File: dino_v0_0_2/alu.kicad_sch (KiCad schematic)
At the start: 22 parts, among them U38 74F382N, U40 74F382N, U45 74LS373, U46 74LS373, U47 74LS373, U48 74LS157, U49 74LS273, U50 74LS02, U52 74LS02, U53 74LS08, U77 74LS157

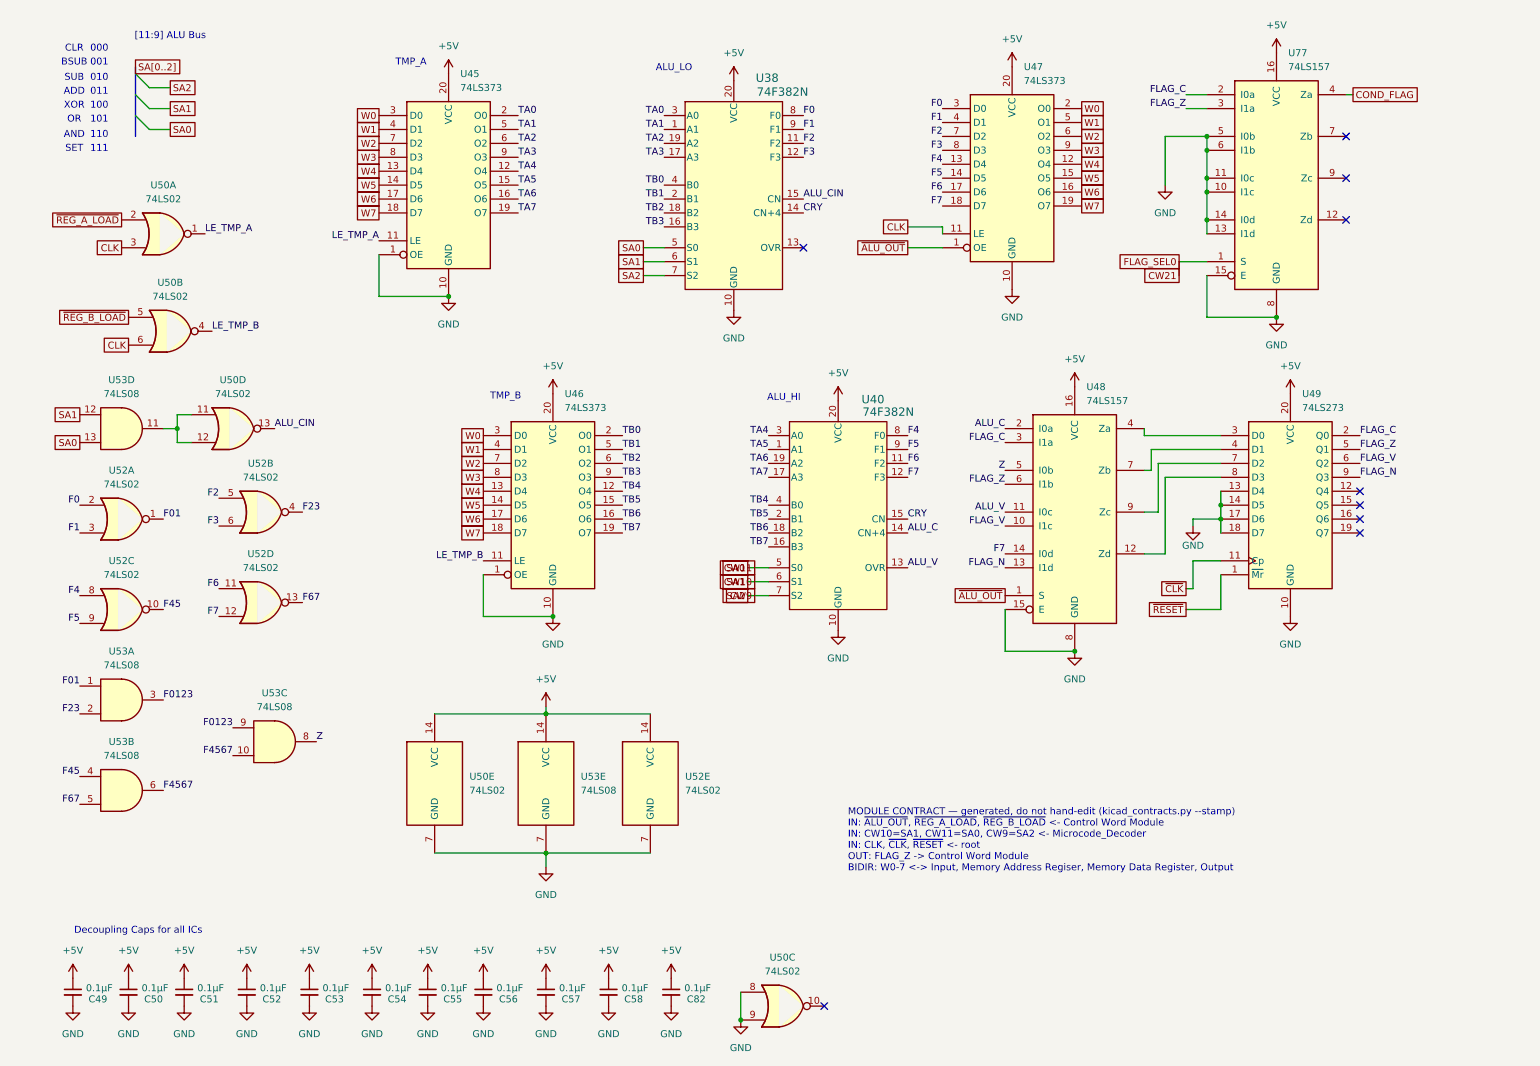
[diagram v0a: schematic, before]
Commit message: feat(int): draw the interrupt block; sheet cleanup pass
New sheet dino_v0_0_2/interrupt.kicad_sch (page 15): U80-U87, R28 4.7k
pull-up on ~{IRQ}, R29 100R on the block's CLK branch, C83-C90. Every
pin per PHASE_INT SECTION 3, checked against the plan with kicad_netlist
and kicad-cli (146 pins, 0 mismatches).

Old sheets (SECTION 3.2): U28.4 lifted off GND to INJECT; U61.3 to
END_OR_ACCEPT; U36.1 to PC_UP_GATED; U49 D0-3 cut from U48 Za-Zd and
routed through U87 as FLAG_NEXT0-3 / FLAG_D0-3; FLAG_C/Z/V/N and the
five decoder outputs made global. dino_serial: U104 74LS05, INTR ->
~{IRQ}, C4.

Placement pass on every sheet: bus entries and global labels no longer
share wires; M, CW, T, IRB and SA buses kept as labelled keys. Nets
diffed against HEAD per sheet: only the intended changes and a rotated
C29. Project ERC: 0 errors. MODULE CONTRACT stamps regenerated.

Co-Authored-By: Claude Fable 5.1 <noreply@anthropic.com>
Claude-Session: https://claude.ai/code/session_01JGxSS4MVUcaZdKZGtKroSg
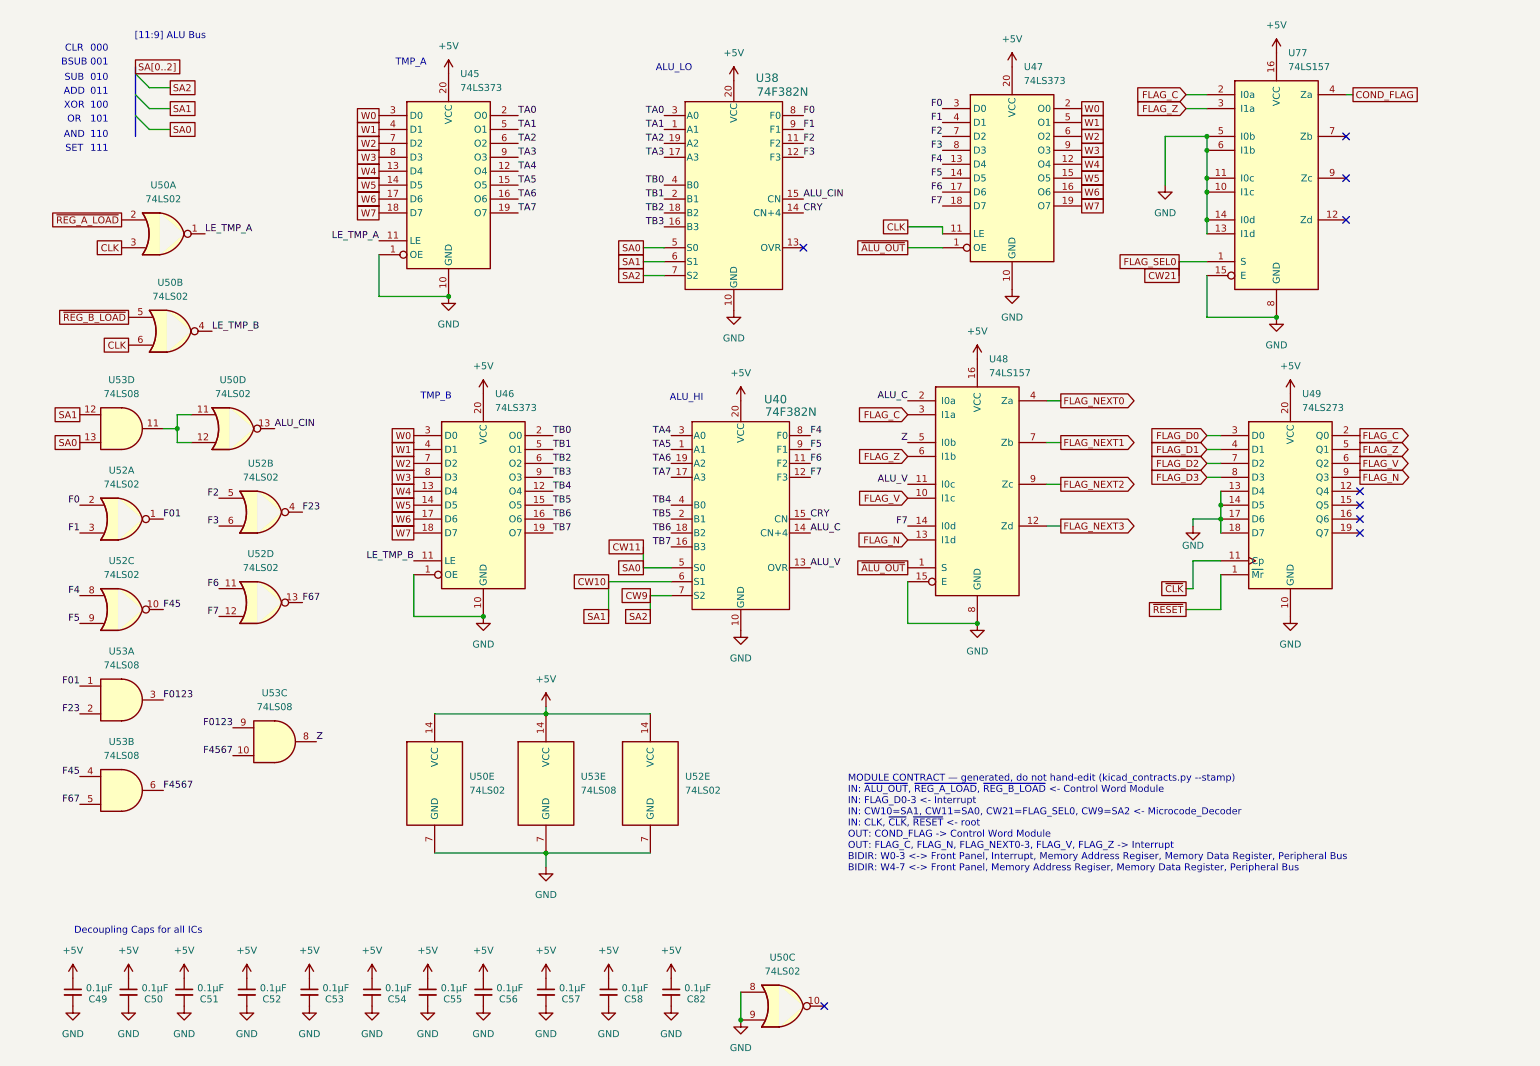
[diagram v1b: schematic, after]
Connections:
- net FLAG_D0: now reaches U49.3 (D0)
- net FLAG_D0: no longer U48.4 (Za)
- net FLAG_D1: now reaches U49.4 (D1)
- net FLAG_D1: no longer U48.7 (Zb)
- net FLAG_D2: now reaches U49.7 (D2)
- net FLAG_D2: no longer U48.9 (Zc)
- net FLAG_D3: now reaches U49.8 (D3)
- net FLAG_D3: no longer U48.12 (Zd)
- new net FLAG_NEXT0: U48.4 (Za)
- new net FLAG_NEXT1: U48.7 (Zb)
- new net FLAG_NEXT2: U48.9 (Zc)
- new net FLAG_NEXT3: U48.12 (Zd)
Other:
- note added: "MODULE CONTRACT — generated, do not hand-edit (kicad_contracts.py --stamp) IN: ~{ALU_OUT}, ~{REG_A_LOAD}, ~{REG_B_LOAD} <- Control Word Module IN: FLAG_D0-3 <- Interrupt IN: CW10=SA1, CW11=SA0, CW21=FLAG_SEL0, CW9=SA2 <- Microcode_Decoder IN: CLK, ~{CLK}, ~{RESET} <- root OUT: COND_FLAG -> Control Word Module OUT: FLAG_C, FLAG_N, FLAG_NEXT0-3, FLAG_V, FLAG_Z -> Interrupt BIDIR: W0-3 <-> Front Pan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"
- note removed: "MODULE CONTRACT — generated, do not hand-edit (kicad_contracts.py --stamp) IN: ~{ALU_OUT}, ~{REG_A_LOAD}, ~{REG_B_LOAD} <- Control Word Module IN: CW10=SA1, CW11=SA0, CW9=SA2 <- Microcode_Decoder IN: CLK, ~{CLK}, ~{RESET} <- root OUT: FLAG_Z -> Control Word Module BIDIR: W0-7 <-> Input, Memory Address Regiser, Memory Data Register, Output"
- moved on the sheet: U40, U46, U48

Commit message: feat(int): ALU latch race fixed, interrupt ladder passes, PROG_imon
The I0 failure after the interrupt build was a same-edge race: U47 (ALU
output '373) took raw CLK at the end of the ALU jumper and closed late
while TMP_A opened on the same CLK fall, so ALU->A rows latched part of
the next result. U47's LE now comes from ~CLK through U37 inverter 5
(net CLK_ALU, mdr + alu sheets, ERC no new violations).

With U104 and the ~IRQ jumper wired, every rung of PHASE_INT section 4
passes at 1.024 MHz. New images: intcount (I3 read off the terminal),
intaddrsw (I4 with SW1 sliding the THRE window), and PROG_imon, the
monitor with input on the RDA interrupt, a 16-byte ring and Ctrl-C
break; putc/puthex/puts/crlf stay at the polling monitor's addresses.
asm/ram/spin.asm is the Ctrl-C witness.

Oracle (test doubles): serial_gap paces scripted RX, the RDA interrupt
is a level, and an interrupt-mode idle rule. test_intser uses the level.
docs/la_caps holds the 2026-10-06 logic analyzer captures.

Co-Authored-By: Claude Opus 5.5 <noreply@anthropic.com>
Claude-Session: https://claude.ai/code/session_01JGxSS4MVUcaZdKZGtKroSg
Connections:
- net CLK: no longer U47.11 (LE)
- new net CLK_ALU: U47.11 (LE)
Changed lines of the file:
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@@
 		)
 	)
-	(global_label "CLK"
+	(global_label "CLK_ALU"
 		(shape passive)
 		(at 170.18 52.07 180)
@@
 		)
 		(property "Intersheetrefs" "${INTERSHEET_REFS}"
-			(at 170.18 52.07 180)
+			(at 160.3232 52.07 0)
 			(hide yes)
 			(show_name no)

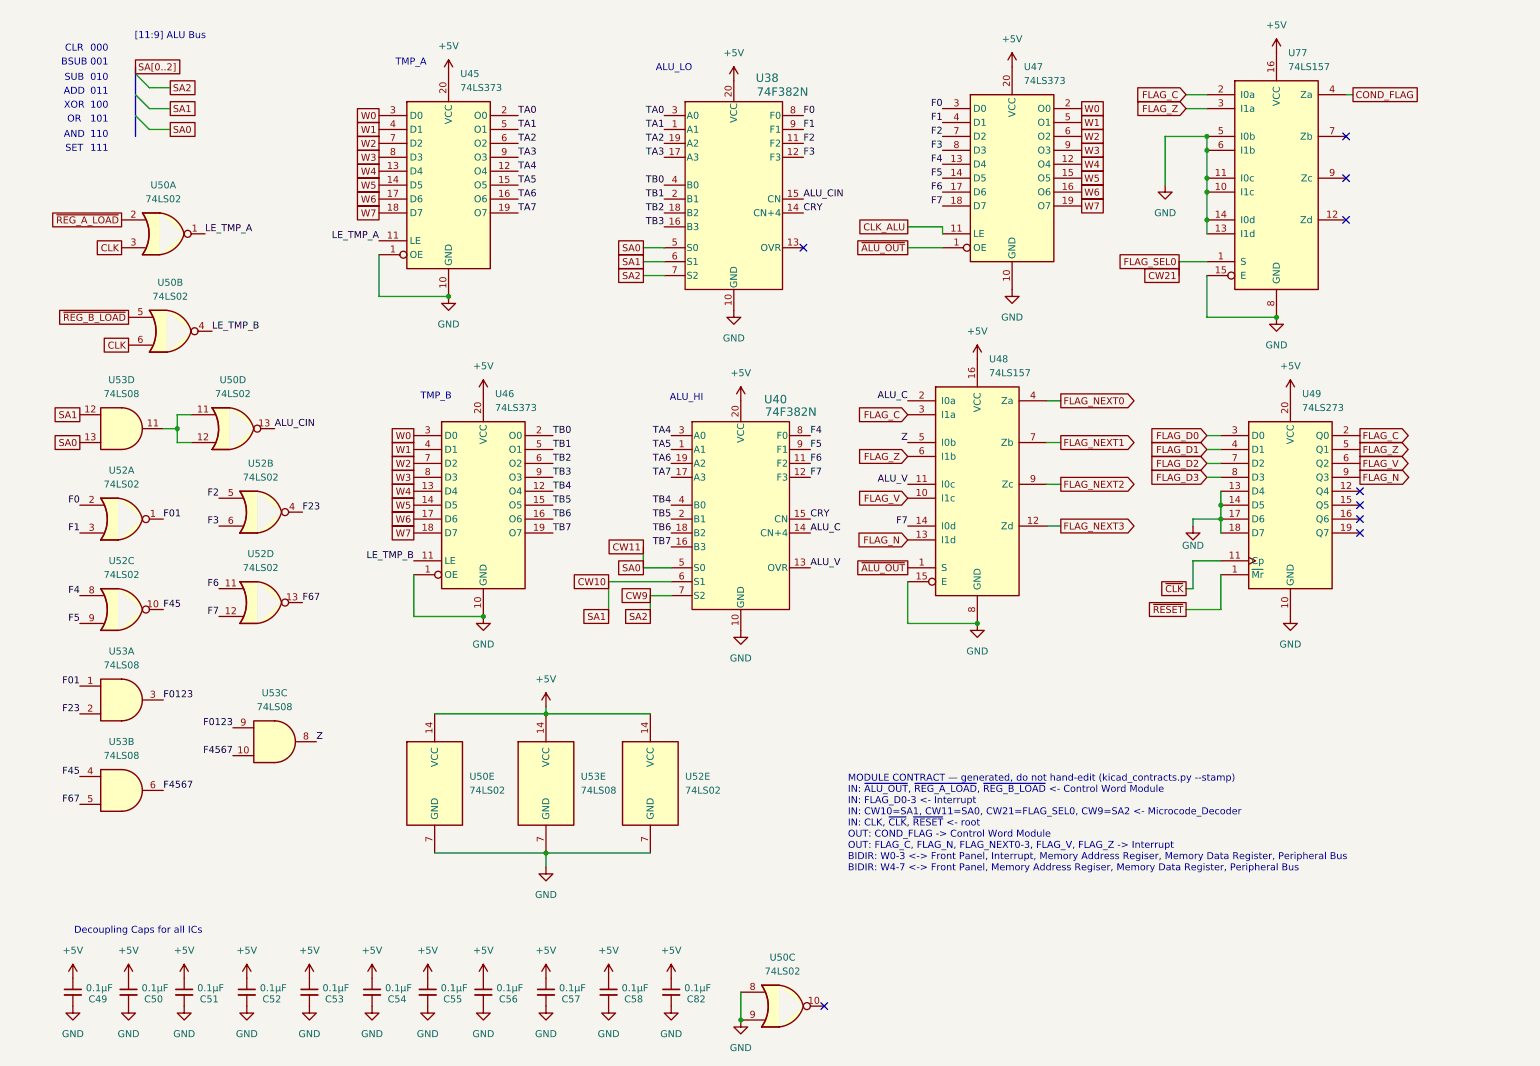
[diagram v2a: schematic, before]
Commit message: feat(alu): ADC/SBB/ACI/SBI through U76, carry microcode burned
U76 ('157, ALU board) picks the '382's CN: S <- CW16 (U23.11),
I0a <- FLAG_C (U49.2), I1a <- ALU_CIN (U50.13), Za -> ALU_CN (U38.15).
CW16 is low only on the ALU rows of 0x96 ADC, 0x97 SBB, 0x98 ACI,
0x99 SBI; check_word refuses it off src=ALU or on a logic code, and the
oracle refuses a carry left by a logic op.

Microcode U9 0x4102 U15 0x9BC4 U23 0x8A40; every row outside 0x96-0x99
is byte-identical to the 0x0C0A interrupt image (test_carry pins it).
PROG_carry (0xCA1F) runs 12 subtests x 256 passes, OB 0xAD.

Bench 2026-10-06, 1.024 MHz on U20.14: with the old microcode isa 0xB4,
isasoak 0x00 x10 (after U76.15 was found loose: isa 0x01); burned:
isa 0xB4 x10, isasoak 0x00 x10, carry 0xAD x10.

Co-Authored-By: Claude Opus 5.5 <noreply@anthropic.com>
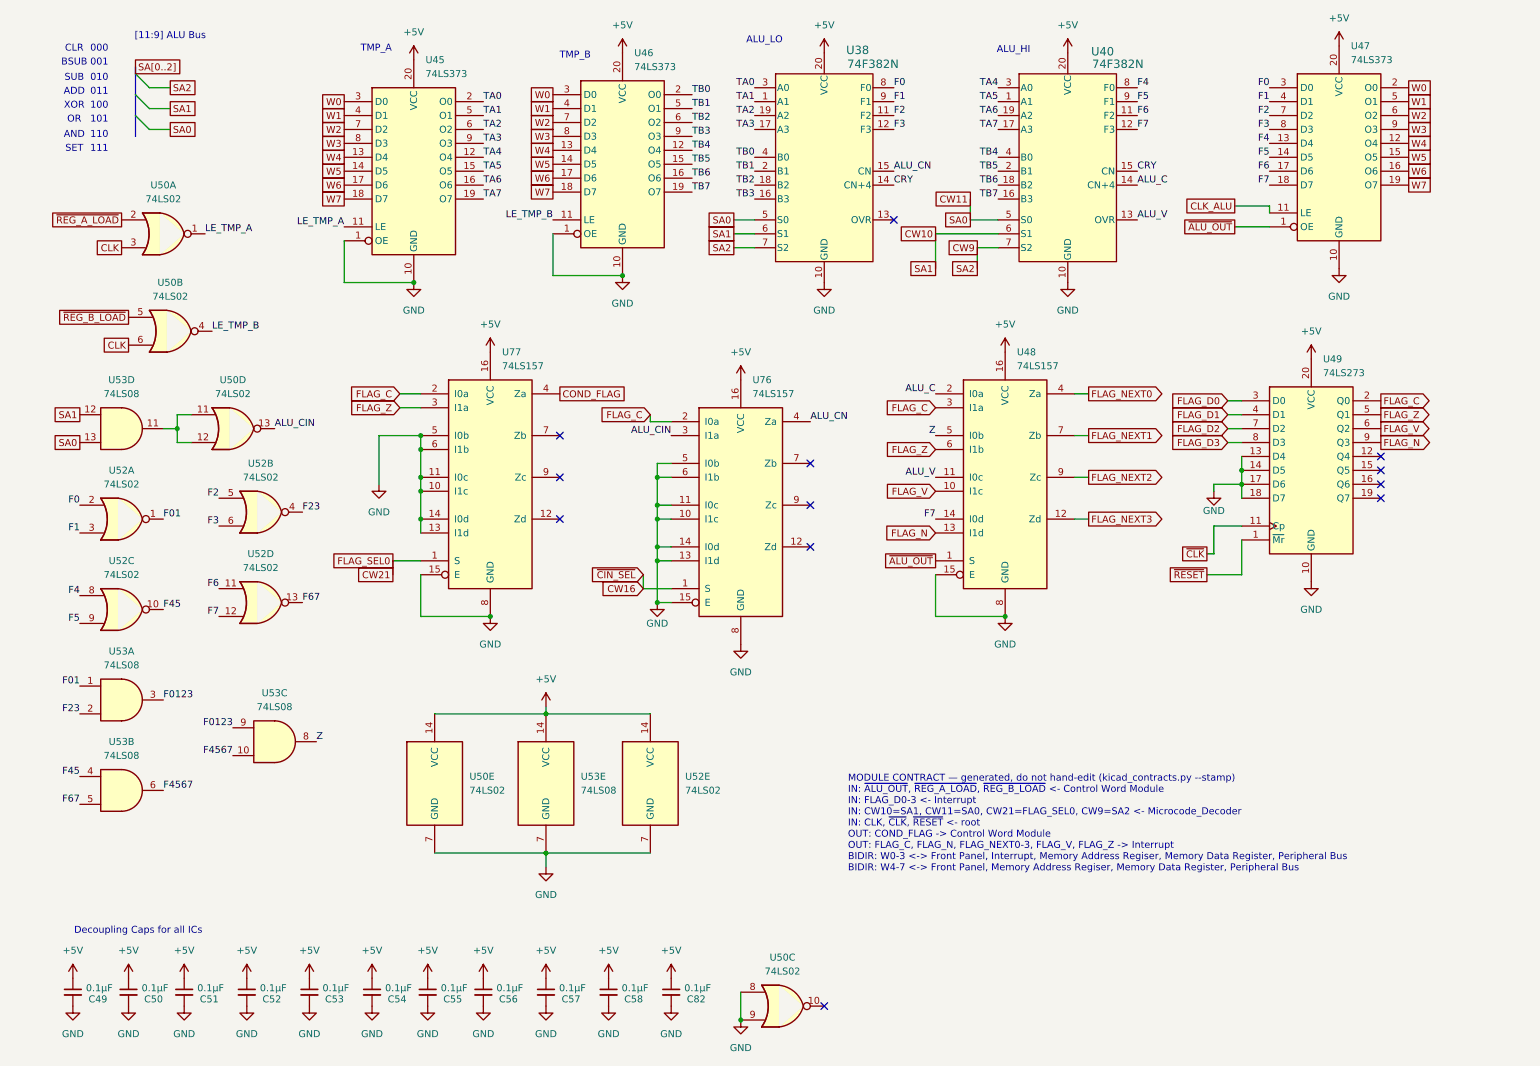
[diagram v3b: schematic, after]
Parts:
- added U76: 74LS157, Package_DIP:DIP-16_W7.62mm, symbol 74xx:74LS157
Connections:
- net +5V: now also U76.16 (VCC)
- net ALU_CIN: now also U76.3 (I1a); no longer U38.15 (CN)
- net FLAG_C: now also U76.2 (I0a)
- net GND: now also U76.10 (I1c), U76.11 (I0c), U76.13 (I1d), U76.14 (I0d), U76.15 (E), U76.5 (I0b), U76.6 (I1b), U76.8 (GND)
- new net ALU_CN: U38.15 (CN), U76.4 (Za)
- new net CW16: U76.1 (S)
- no-connect marks 9 -> 12
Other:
- moved on the sheet: U38, U40, U45, U46, U47, U48, U49, U77
